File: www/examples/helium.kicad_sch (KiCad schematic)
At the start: 64 parts, among them J1 Power, J10 OUT B3, J12 IN C, J13 OUT C1, J14 OUT C2, J15 OUT C3, J17 OUT D, J18 IN D1, J19 IN D2, J2 IN A, J20 IN D3, J3 OUT A1, J4 OUT A2, J5 OUT A3, J7 IN B, J8 OUT B1, J9 OUT B2, U1 OPA4991, U2 OPA4991, U4 OPA4991, U6 OPA4991

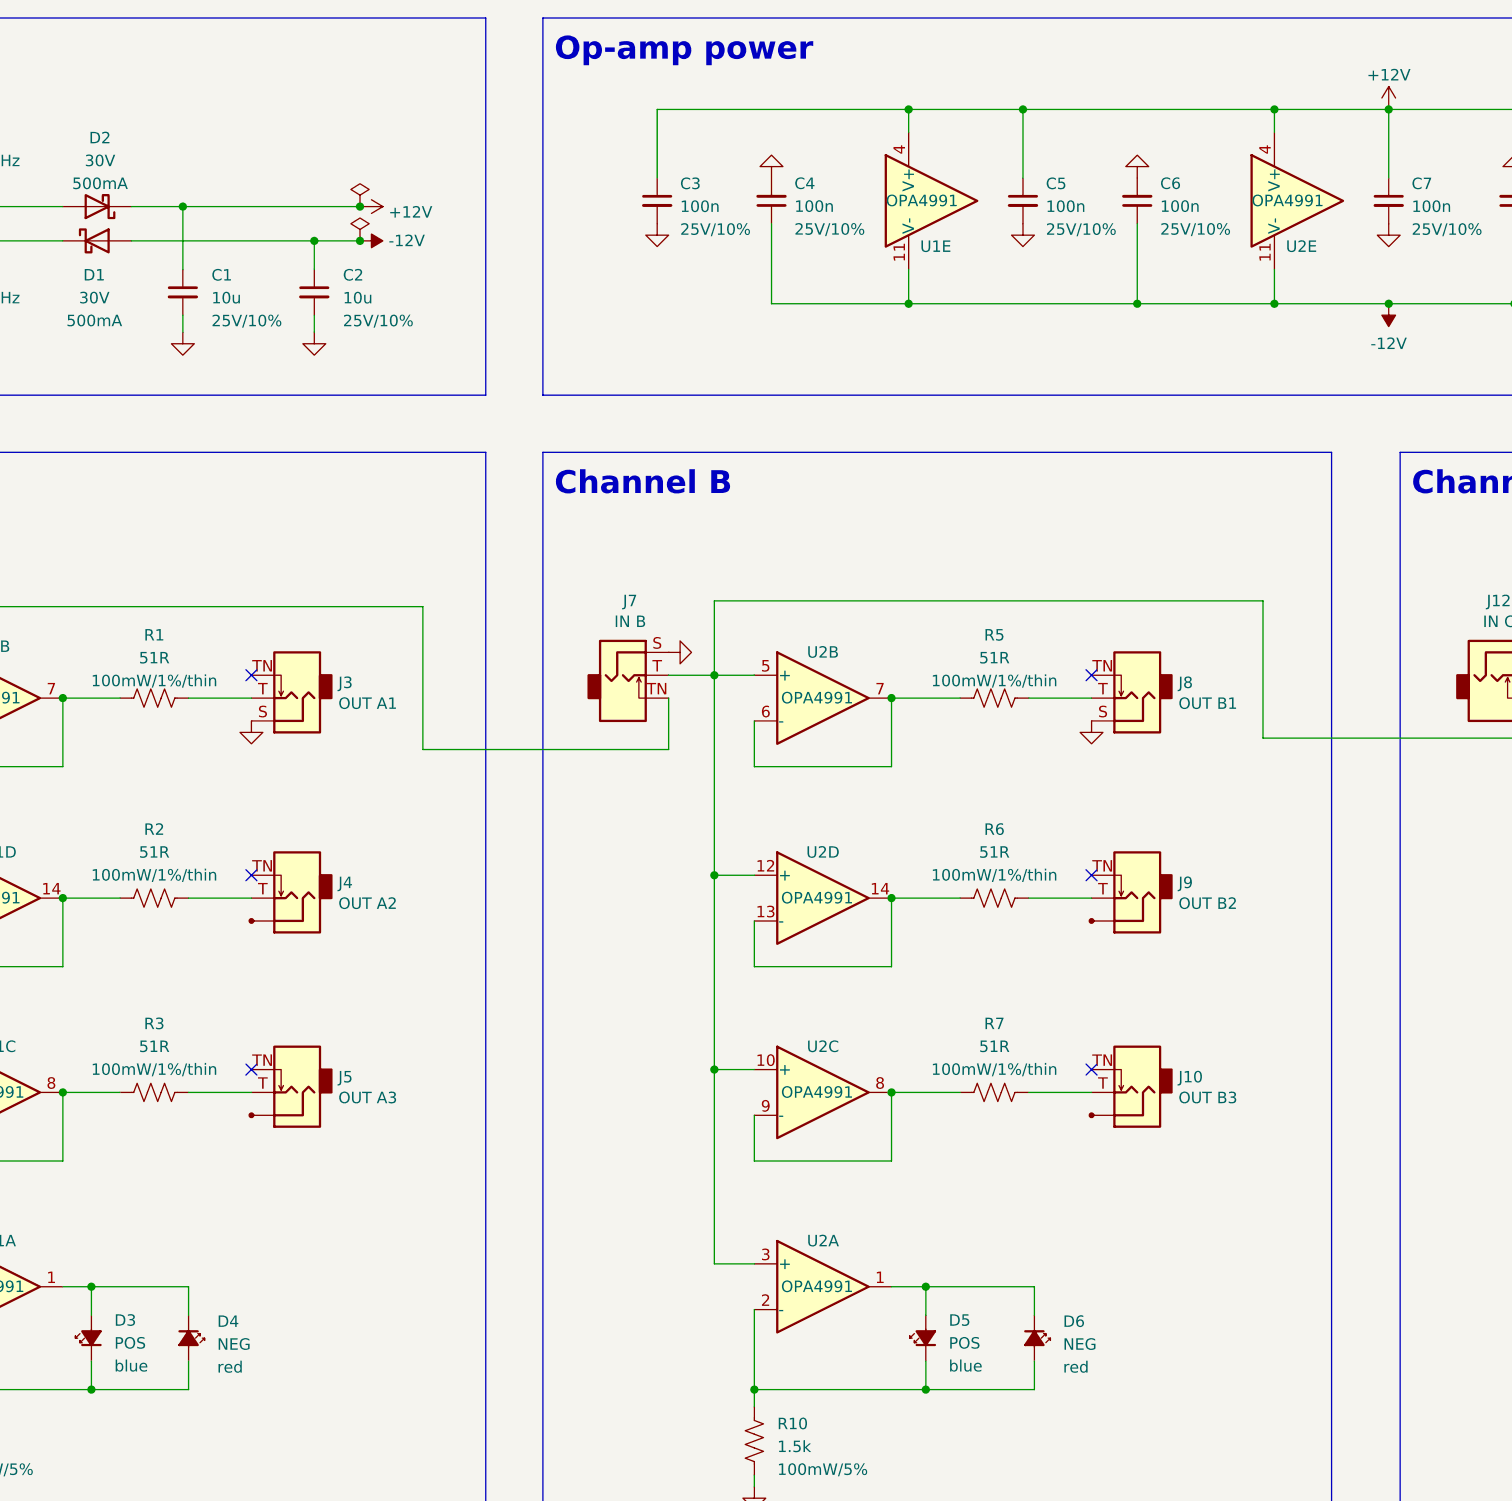
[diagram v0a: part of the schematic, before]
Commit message: Update helium example to include DNP
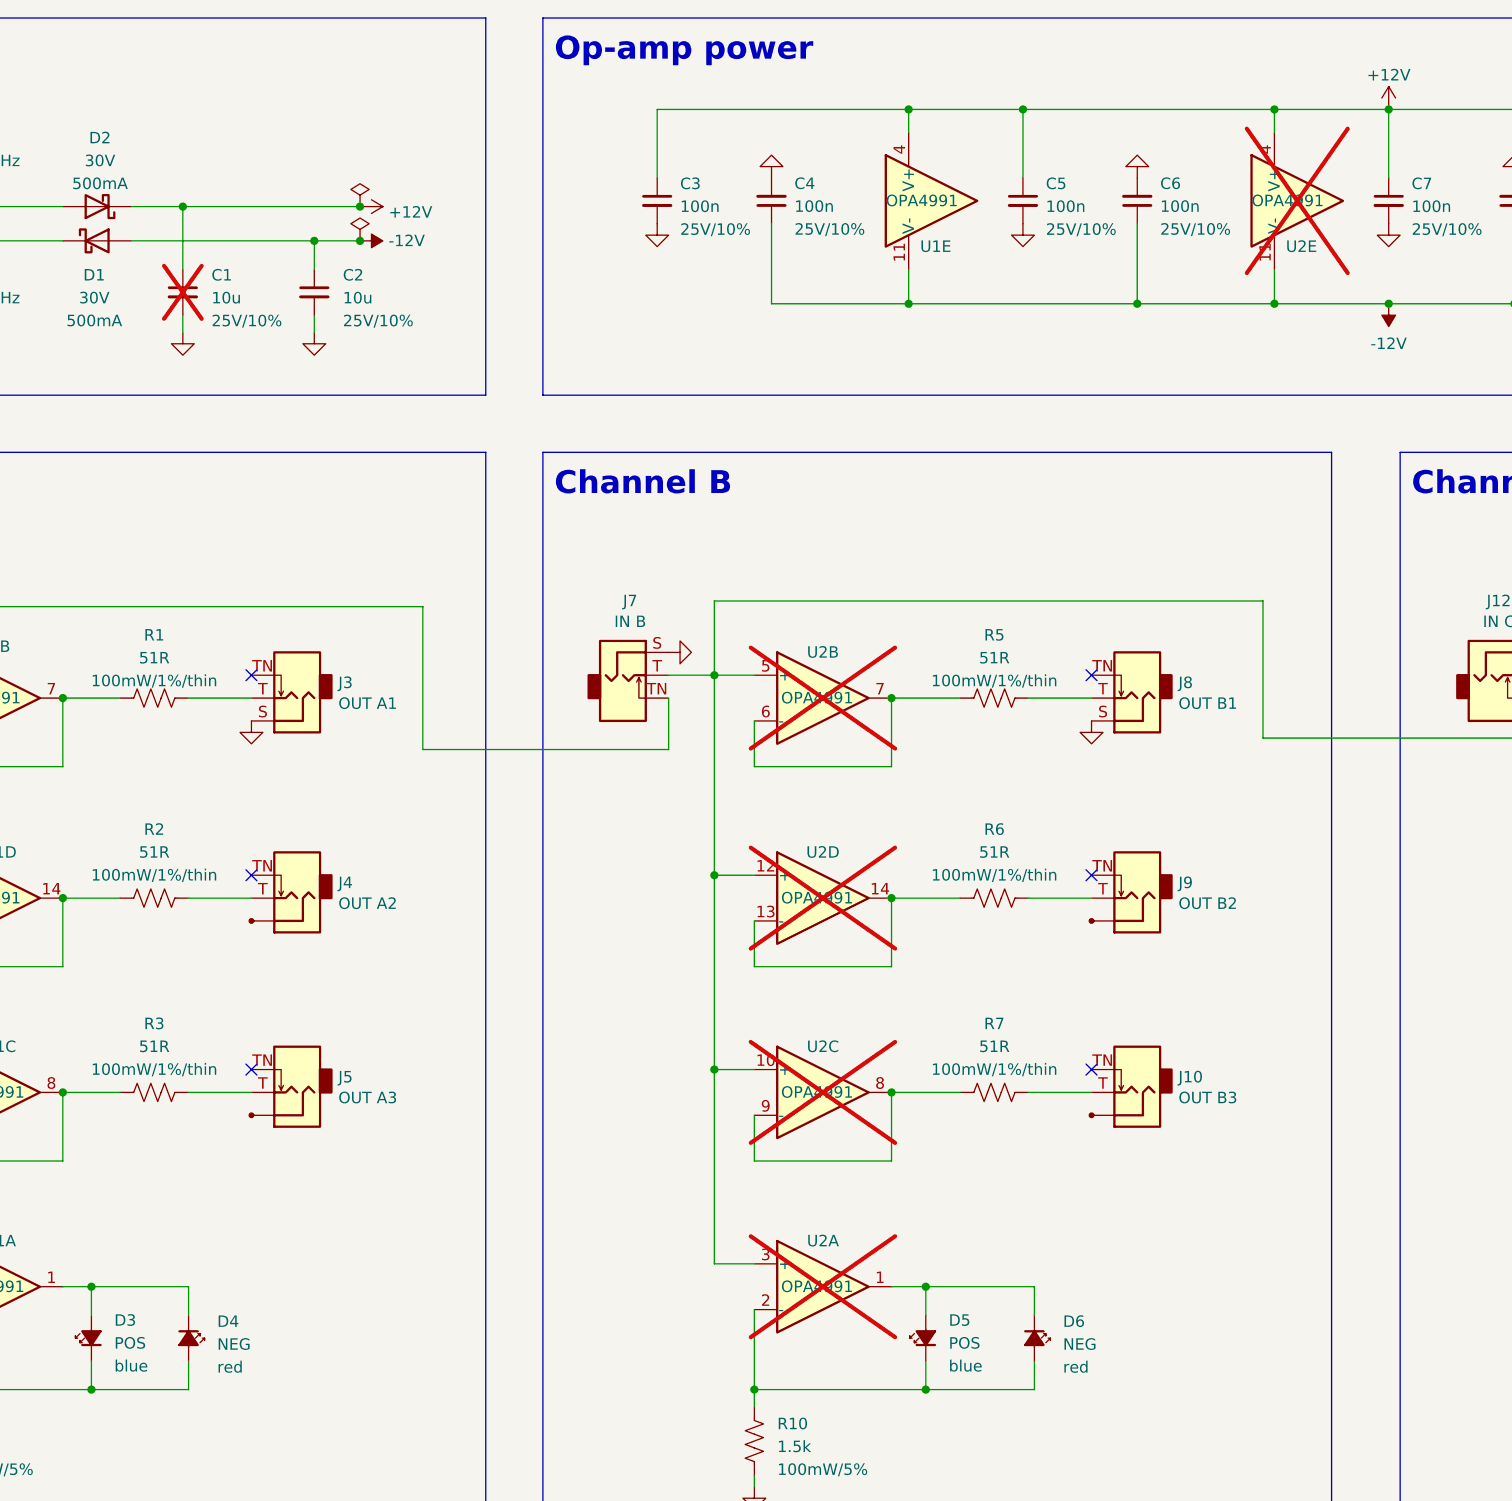
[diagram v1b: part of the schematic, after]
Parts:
- C1, U2: now not fitted
